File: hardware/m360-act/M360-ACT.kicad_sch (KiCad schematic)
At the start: 26 parts, among them J1 5V do quadro, J2 M360-RF, J3 RJ45 RELES-A, J4 RJ45 RELES-B, J5 RJ45 SENSORES, SW1 Repareamento, U1 AMS1117-3.3, U2 74HCT244, U3 CD74HC4067, U4 SRV05-4, U5 SRV05-4, U6 SRV05-4, U7 SRV05-4, U8 SRV05-4

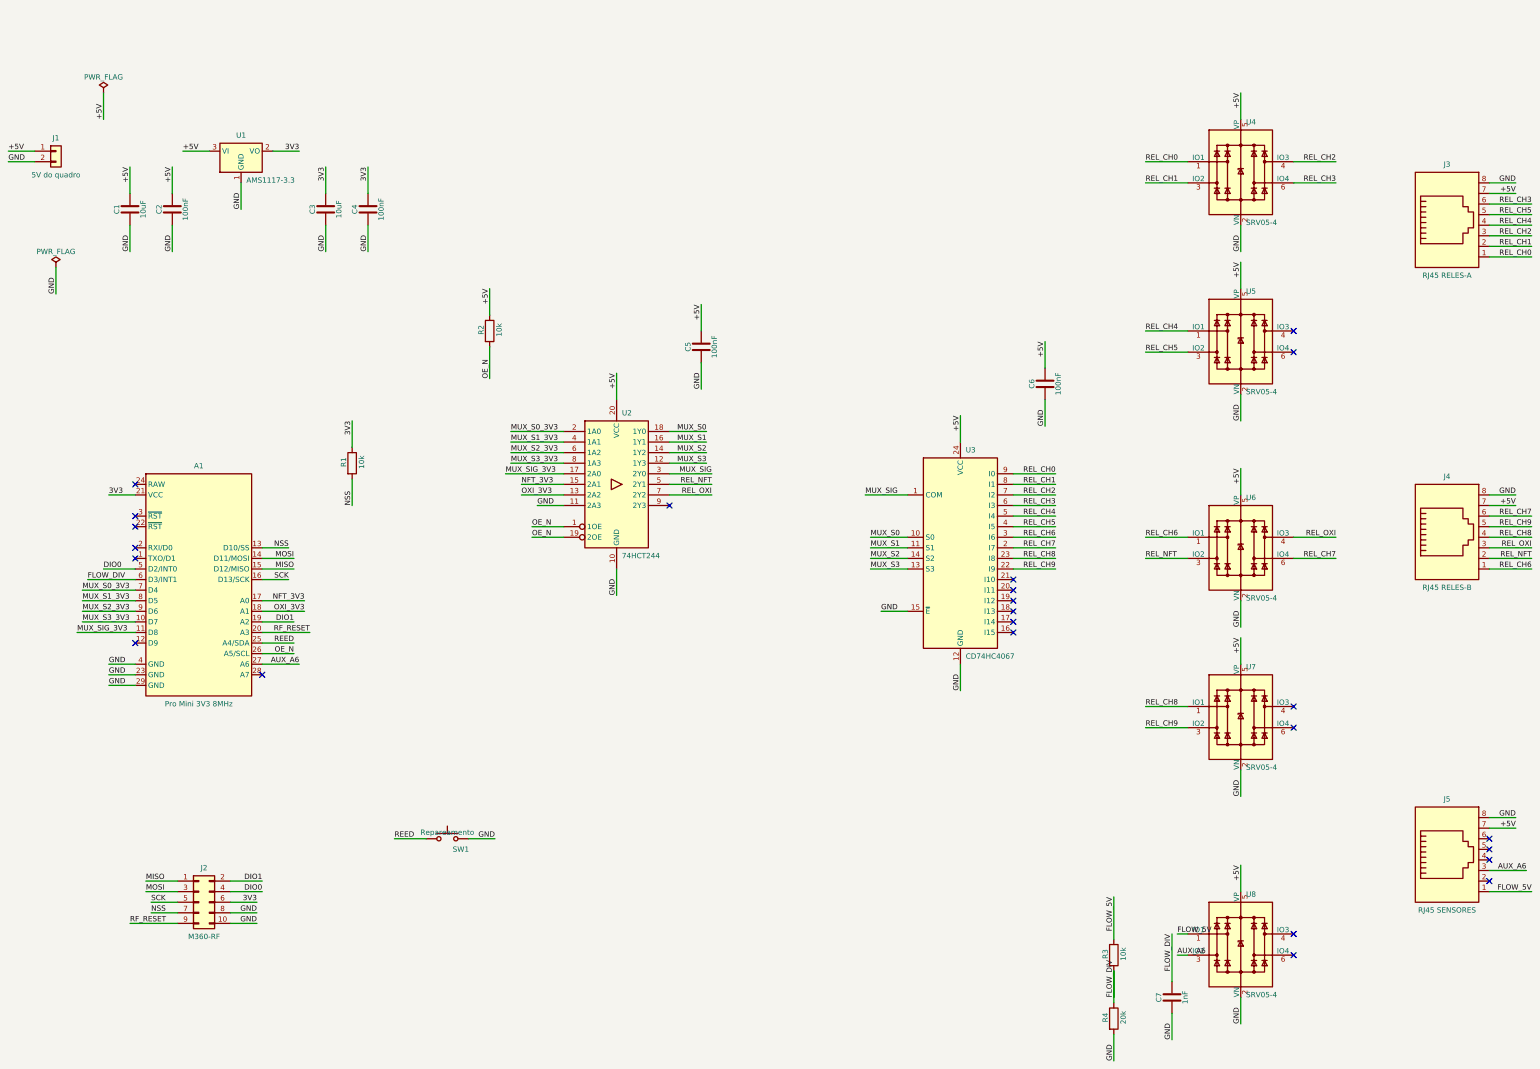
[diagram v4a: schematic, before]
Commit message: feat(hardware): esquemáticos corrigidos após análise adversarial; reed nas três placas; GW em SMD
⚠️ **Só esquemáticos.** Os três .kicad_pcb estão defasados e serão refeitos depois de uma nova
análise adversarial, até zerar os achados (pedido do usuário). ARQUITETURA §9 registra.

Correções da revisão (Fable 5.1, 2026-09-13):
- ACT #1: A6 da J5 com divisor 10 k (R5) / 20 k (R6) + 100 nF (C8); J5.3 e U8.3 vão para AUX_A6_IN.
  Antes, 5 V do par marrom chegavam direto ao ADC6 de um ATmega a 3,3 V.
- ACT #2: pull-up do /OE (R2) de +5V para 3V3 — A5 em alta impedância ficava a ~3,8 V.
- ACT #4: 7× 100 kΩ — pull-down em MUX_S0..S3, pull-up para 5 V em MUX_SIG/REL_NFT/REL_OXI.
- ACT #6: AMS1117 → ME6211C33M5 (C82942), estável com cerâmico.
- ACT #12: AO3401A (Q1) contra inversão no borne; J1.1 vai para VIN_RAW.
- GW #5/#12: Schottky SS14 (D1, C2480) em série de J2.1 (VIN_RAW) para +5V.
- Achados 3, 7, 8, 9, 10 e 11: documentação e regras de firmware (módulo TP4056 com DW01+8205;
  vazão com INPUT; calibração e analogReference do A6 da LP; chave do mezanino cortando o pino 10;
  FTDI sem VCC; orçamento do 3,3 V da GW).

Decisões do usuário:
- Reed switch Littelfuse 59170 (C315909) de volta na LP e na ACT e **no lugar do botão AP/reset da
  GW**, pela PCBA. Símbolo trocado por texto (pinagem idêntica): netlists idênticas.
- GW em SMD pela JLCPCB: R 0603, C1 10 µF 0805 (`Device:C`), C2–C4 100 nF 0603, códigos basic.
  Solda manual só U1 (D1 mini), J1, J2, J3. Os PWR_FLAG saem do BOM.
- Solda manual marcada só nos esquemáticos (`solda_manual.py --so-esquematico`, e `--desfazer` no
  SW1): LP J3; ACT J1; GW U1, J1, J2, J3.

Verificado nas três: netdiff contra a base lista só as mudanças acima (LP idêntica); campos de
todos os componentes comparados; símbolos de biblioteca embutidos comparados com o HEAD; ERC 0;
BOM com código LCSC em todas as linhas (exceto módulos); desenho conferido em PDF.

Três armadilhas medidas no caminho (ARQUITETURA §12):
- `replace_schematic_component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
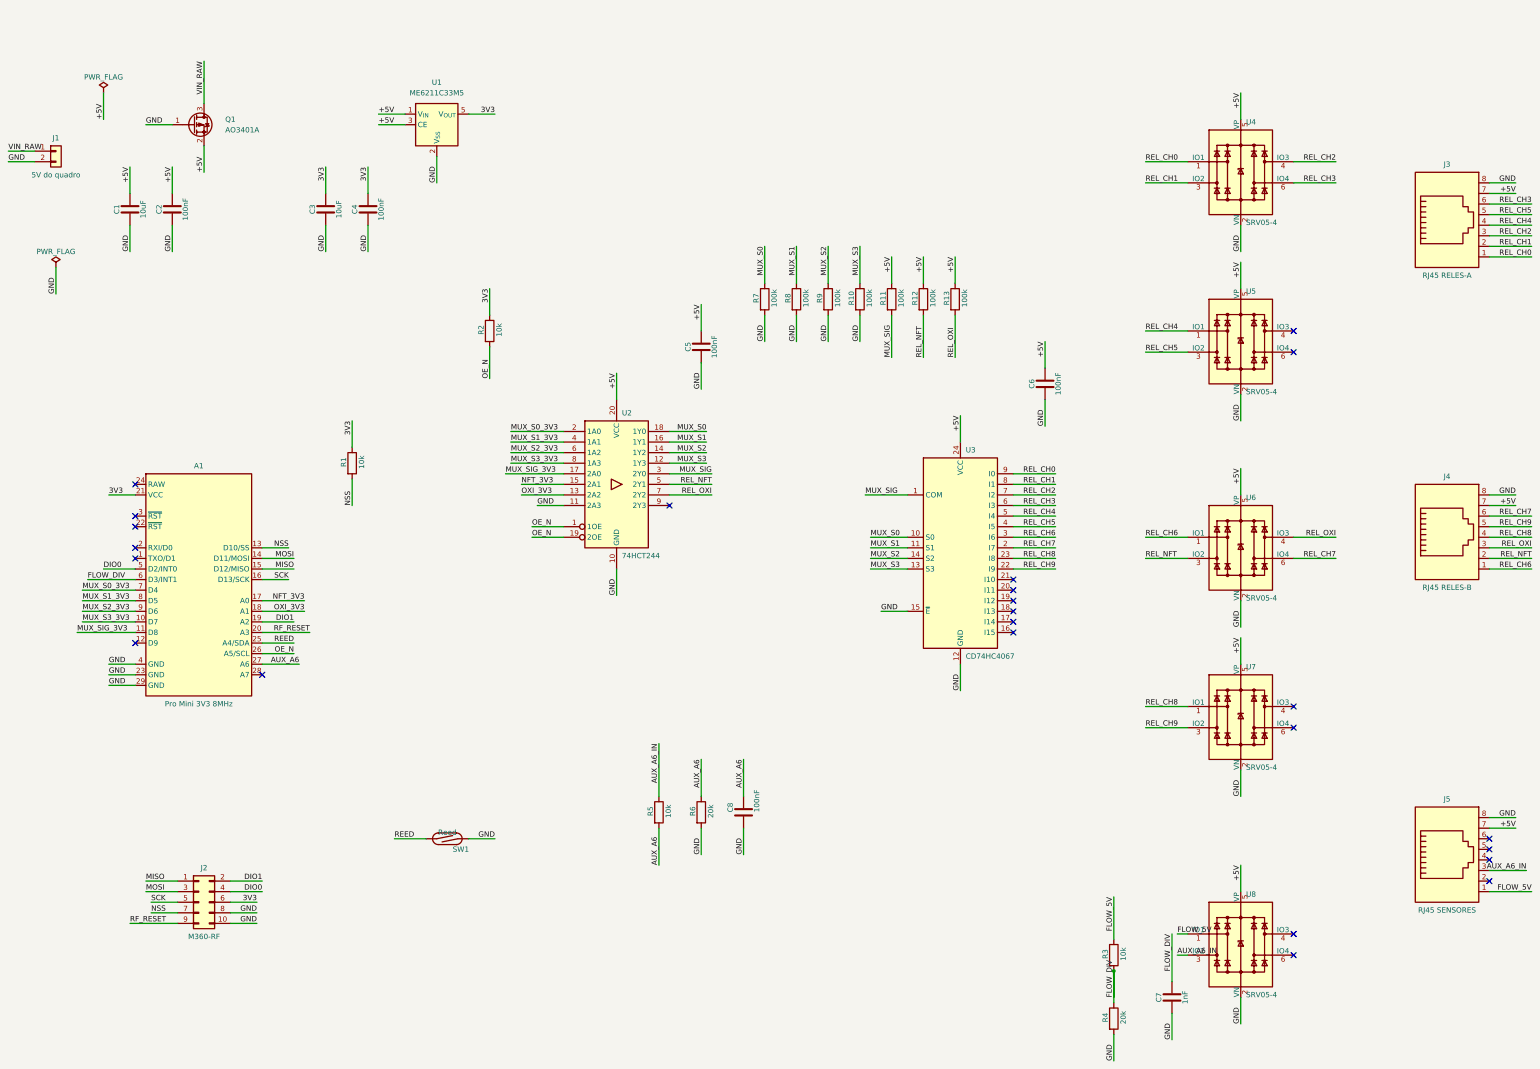
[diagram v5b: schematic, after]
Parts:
- removed U1: AMS1117-3.3, Package_TO_SOT_SMD:SOT-223-3_TabPin2, symbol Regulator_Linear:AMS1117-3.3
- added C8: 100nF, Capacitor_SMD:C_0603_1608Metric, symbol Device:C
- added Q1: AO3401A, Package_TO_SOT_SMD:SOT-23, symbol Transistor_FET:AO3401A
- added R10, R11, R12, R13, R7, R8, R9: 100k, Resistor_SMD:R_0603_1608Metric, symbol Device:R
- added R5: 10k, Resistor_SMD:R_0603_1608Metric, symbol Device:R
- added R6: 20k, Resistor_SMD:R_0603_1608Metric, symbol Device:R
- added U1: ME6211C33M5, Package_TO_SOT_SMD:SOT-23-5, symbol Regulator_Linear:ME6211C33M5
- J1: now left out of the parts list
- SW1: value Repareamento -> Reed; footprint Button_Switch_THT:SW_PUSH_6mm -> M360:Reed_Littelfuse_59170; symbol Switch:SW_Push -> Switch:SW_Reed; LCSC C393938 -> C315909; now in the parts list
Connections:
- net +5V: now also Q1.2 (S), R11.1, R12.1, R13.1, U1.1 (V_{IN}), U1.3 (CE); no longer J1.1 (Pin_1), R2.1
- net 3V3: now also R2.1, U1.5 (V_{OUT})
- net AUX_A6: now also C8.1, R5.2, R6.1; no longer J5.3, U8.3 (IO2)
- net GND: now also C8.2, Q1.1 (G), R10.2, R6.2, R7.2, R8.2, R9.2, U1.2 (V_{SS})
- net MUX_S0: now also R7.1
- net MUX_S1: now also R8.1
- net MUX_S2: now also R9.1
- net MUX_S3: now also R10.1
- net MUX_SIG: now also R11.2
- net REL_NFT: now also R12.2
- net REL_OXI: now also R13.2
- new net AUX_A6_IN: J5.3, R5.1, U8.3 (IO2)
- new net VIN_RAW: J1.1 (Pin_1), Q1.3 (D)

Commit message: fix(hardware): esquemáticos — correções da 2ª análise adversarial
⚠️ Só esquemáticos; as placas continuam defasadas de propósito até zerar os achados.

- LP #1 (firmware + documento): a referência DEFAULT é o VCC, e abaixo de ~3,31 V de bateria o
  MCP1700 sai de regulação — o A6 devolve sempre "3,3 V". O firmware corrige pelo VCC medido no
  bandgap (`readADCInternal()` de M360Power.cpp): VBAT = 3 × ADC_A6 × VCC / 1023. §4.1 e §9.
- ACT #2: entrada da vazão refeita — R3 10 kΩ em série, D1 BAT54WS (C7502694) do D3 para o 3V3,
  R4 de 20 kΩ para 100 kΩ (pull-down, sem pulsos falsos com o sensor desligado). Serve às unidades
  push-pull e às de coletor aberto com pull-up interno, que no divisor antigo davam só 2,5 V.
- ACT #3: R14–R20 100 kΩ nas entradas do 74HCT244 — pull-down em MUX_S0..S3_3V3, pull-up para 3V3
  em MUX_SIG_3V3, NFT_3V3 e OXI_3V3. O /OE cobria as saídas, não as entradas.
- GW #4: Q1 2N7002 (C8545) — o GPIO2 (boot) só comanda o gate; o LED verde vai do 3,3 V ao dreno.
  Curto do chicote para o GND acende o LED em vez de travar o boot. Verde passa a ativo em HIGH,
  como os outros — some a inversão pendente no M360Leds.cpp.
- ACT #5: nota de projeto — o divisor do A6 carrega a fonte com 30 kΩ (§5.2, §7).
- Documento: `MY_RFM95_RST_PIN` (D8 na LP, A3 na ACT) na §9; saem a linha "DHT11 no atuador" da §9
  e o buck XL1509 da §9.1, inconsistentes com a §5.

Verificado: netdiff contra o commit anterior só com as redes previstas (LP idêntica; ACT 10, GW 3);
campos dos componentes existentes inalterados (fora o valor do R4); símbolos de biblioteca
existentes inalterados; ERC 0 nas três; BOM com código LCSC em todas as linhas; desenho conferido
em PDF.

Co-Authored-By: Claude Opus 5 (1M context) <noreply@anthropic.com>
Claude-Session: https://claude.ai/code/session_012t7RkcrXvvpDVjKVimNu18
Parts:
- added D1: BAT54WS, Diode_SMD:D_SOD-323, symbol Device:D_Schottky
- added R14, R15, R16, R17, R18, R19, R20: 100k, Resistor_SMD:R_0603_1608Metric, symbol Device:R
- R4: value 20k -> 100k; LCSC C4184 -> C25803
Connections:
- net 3V3: now also D1.1 (K), R18.1, R19.1, R20.1
- net FLOW_DIV: now also D1.2 (A)
- net GND: now also R14.2, R15.2, R16.2, R17.2
- net MUX_S0_3V3: now also R14.1
- net MUX_S1_3V3: now also R15.1
- net MUX_S2_3V3: now also R16.1
- net MUX_S3_3V3: now also R17.1
- net MUX_SIG_3V3: now also R18.2
- net NFT_3V3: now also R19.2
- net OXI_3V3: now also R20.2

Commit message: fix(hardware): esquemáticos — correções da 3ª análise adversarial
⚠️ Só esquemáticos; as placas continuam defasadas de propósito até zerar os achados.

- LP #1: 100 Ω em série (R26–R29, C22775) entre o TVS e o Pro Mini nas linhas de campo digitais.
  A1.18/19/25/26 passam às redes ONEWIRE_MCU, DHT_MCU, SDA_MCU e SCL_MCU; pull-ups e TVS ficam do
  lado do conector. O pino do ATmega deixa de dividir o surto com o TVS.
- ACT #2: 100 Ω em série (R21–R32) entre o CI e o TVS nas 12 linhas de relé — U3 I0–I9 em
  REL_CHx_MUX, U2 2Y1/2Y2 em REL_NFT_BUF/REL_OXI_BUF. Custa 0,2 V nos 2 mA do opto.
- ACT e GW #3: TVS SMAJ5.0A (D2, C2925443) do +5V ao GND, depois do Q1 (ACT) e do D1 (GW), contra
  DC-DC ajustável girado por engano. Símbolo `Device:D_Zener` — o `D_TVS` do KiCad é bidirecional.
- GW #4: nota — o LED azul do D1 mini no GPIO2 fica invertido em relação ao verde do painel.
- Regras: limiar de corte de TX ≥ 3,0 V por causa do BOD de 2,7 V (efuse 0xFD); confirmar os fuses
  dos clones DeeKRobot por ISP; `initLEDs` com argumentos trocados continua registrado. §9.

Verificado: netdiff contra o commit anterior só com as redes previstas (LP 8, ACT 26, GW 2);
campos dos componentes existentes inalterados; símbolos de biblioteca existentes inalterados
(entra só o D_Zener, sai o D_TVS); ERC 0; BOM com código LCSC em todas as linhas; desenho
conferido em PDF. O diff da LP é grande porque o arquivo passou pela primeira vez por
`kicad-cli sch upgrade --force` (§12).

No caminho: o MCP ignorou o ângulo pedido em `add_schematic_component` (todas as peças entraram em
rot 0) e, com as fileiras apertadas, os fios desenhados fundiram redes — o netdiff e o ERC pegaram,
e a geometria foi refeita antes do commit.

Co-Authored-By: Claude Opus 5 (1M context) <noreply@anthropic.com>
Claude-Session: https://claude.ai/code/session_012t7RkcrXvvpDVjKVimNu18
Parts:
- added D2: SMAJ5.0A, Diode_SMD:D_SMA, symbol Device:D_Zener
- added R21, R22, R23, R24, R25, R26, R27, R28, R29, R30, R31, R32: 100, Resistor_SMD:R_0603_1608Metric, symbol Device:R
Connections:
- net +5V: now also D2.1 (K)
- net GND: now also D2.2 (A)
- net REL_CH0: now also R21.2; no longer U3.9 (I0)
- net REL_CH1: now also R22.2; no longer U3.8 (I1)
- net REL_CH2: now also R23.2; no longer U3.7 (I2)
- net REL_CH3: now also R24.2; no longer U3.6 (I3)
- net REL_CH4: now also R25.2; no longer U3.5 (I4)
- net REL_CH5: now also R26.2; no longer U3.4 (I5)
- net REL_CH6: now also R27.2; no longer U3.3 (I6)
- net REL_CH7: now also R28.2; no longer U3.2 (I7)
- net REL_CH8: now also R29.2; no longer U3.23 (I8)
- net REL_CH9: now also R30.2; no longer U3.22 (I9)
- net REL_NFT: now also R31.2; no longer U2.5 (2Y1)
- net REL_OXI: now also R32.2; no longer U2.7 (2Y2)
- new net REL_CH0_MUX: R21.1, U3.9 (I0)
- new net REL_CH1_MUX: R22.1, U3.8 (I1)
- new net REL_CH2_MUX: R23.1, U3.7 (I2)
- new net REL_CH3_MUX: R24.1, U3.6 (I3)
- new net REL_CH4_MUX: R25.1, U3.5 (I4)
- new net REL_CH5_MUX: R26.1, U3.4 (I5)
- new net REL_CH6_MUX: R27.1, U3.3 (I6)
- new net REL_CH7_MUX: R28.1, U3.2 (I7)
- new net REL_CH8_MUX: R29.1, U3.23 (I8)
- new net REL_CH9_MUX: R30.1, U3.22 (I9)
- new net REL_NFT_BUF: R31.1, U2.5 (2Y1)
- new net REL_OXI_BUF: R32.1, U2.7 (2Y2)

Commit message: fix(hardware): PTC na entrada de 5 V da ACT e da GW — correções da 4ª análise adversarial
⚠️ Só esquemáticos; as placas continuam defasadas de propósito até zerar os achados.

- ACT e GW #1: PTC F1 500 mA / 30 V (Jinrui JK-nSMD050-30, C720075) em série na entrada, depois do
  Q1 (ACT) e do SS14 (GW) e antes do TVS D2 — Q1.2 e D1.1 passam à rede VIN_POL. A ruptura mínima
  do SMAJ5.0A (6,4 V) fica acima da dos SRV05-4 (6,0 V), então sozinho o D2 não tirava os TVS de
  sinal do papel sacrificial; com o F1 a montante, a condução do D2 abre o circuito. O F1 cobre
  também o curto no chicote (a placa desarma, o quadro não cai) — §9 revista.
  Escolhido no lugar do SMD1206P050TF/15 (C106264) sugerido: mesma especificação, 427 mil em
  estoque contra 1 350, e resistência máxima de 300 mΩ contra 750 mΩ.
- ACT #2: procedimento — barramento de 5 V do quadro ajustado em 5,0 V (máx. 5,1 V), na §5.1.
- Pino 1 do RJ45: verificado por geometria e convenção pela revisão; registrada na §9 a medida de
  continuidade na primeira placa (branco-laranja T568B ↔ pad 1) antes de crimpar os chicotes.

Verificado: netdiff só com as duas redes previstas em cada placa; campos e símbolos de biblioteca
existentes inalterados (entra o Polyfuse); ERC 0; BOM com código LCSC em todas as linhas; desenho
conferido em PDF.

Co-Authored-By: Claude Opus 5 (1M context) <noreply@anthropic.com>
Claude-Session: https://claude.ai/code/session_012t7RkcrXvvpDVjKVimNu18
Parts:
- added F1: 500mA, Fuse:Fuse_1206_3216Metric, symbol Device:Polyfuse
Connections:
- net +5V: now also F1.2; no longer Q1.2 (S)
- new net VIN_POL: F1.1, Q1.2 (S)
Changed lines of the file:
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@@
 	(wire
 		(pts
+			(xy 66.04 33.02) (xy 66.04 22.86)
+		)
+		(stroke
+			(width 0)
+			(type default)
+		)
+	)
+	(wire
+		(pts
 			(xy 298.45 243.84) (xy 298.45 232.41)
 		)
@@
 	(wire
 		(pts
-			(xy 66.04 33.02) (xy 66.04 22.86)
-		)
-		(stroke
-			(width 0)
-			(type default)
-		)
-	)
-	(wire
-		(pts
-			(xy 66.04 43.18) (xy 66.04 49.53)
-		)
-		(stroke
-			(width 0)
-			(type default)
-		)
-	)
-	(wire
-		(pts
 			(xy 208.28 229.87) (xy 208.28 223.52)
 		)
@@
 	(wire
 		(pts
+			(xy 58.42 38.1) (xy 52.07 38.1)
+		)
+		(stroke
+			(width 0)
+			(type default)
+		)
+	)
+	(wire
+		(pts
 			(xy 327.66 46.99) (xy 337.82 46.99)
 		)
@@
 	(wire
 		(pts
+			(xy 81.28 59.69) (xy 81.28 66.04)
+		)
+		(stroke
+			(width 0)
+			(type default)
+		)
+	)
+	(wire
+		(pts
 			(xy 284.48 241.3) (xy 284.48 247.65)
 		)
@@
 	(wire
 		(pts
-			(xy 58.42 38.1) (xy 52.07 38.1)
-		)
-		(stroke
-			(width 0)
-			(type default)
-		)
-	)
-	(wire
-		(pts
 			(xy 156.21 33.02) (xy 142.24 33.02)
 		)
@@
 	(wire
 		(pts
+			(xy 66.04 43.18) (xy 66.04 53.34)
+		)
+		(stroke
+			(width 0)
+			(type default)
+		)
+	)
+	(wire
+		(pts
 			(xy 152.4 137.16) (xy 144.78 137.16)
 		)
@@
 	(wire
 		(pts
+			(xy 81.28 52.07) (xy 81.28 41.91)
+		)
+		(stroke
+			(width 0)
+			(type default)
+		)
+	)
+	(wire
+		(pts
 			(xy 314.96 62.23) (xy 314.96 68.58)
 		)
@@
 		)
 	)
+	(label "VIN_POL"
+		(at 81.28 41.91 270)
+		(effects
+			(font
+				(size 1.27 1.27)
+			)
+			(justify right bottom)
+		)
+	)
 	(label "MUX_S1_3V3"
 		(at 170.18 217.17 270)
@@
 		)
 	)
-	(label "+5V"
-		(at 66.04 49.53 90)
-		(effects
-			(font
-				(size 1.27 1.27)
-			)
-			(justify left bottom)
-		)
-	)
 	(label "MOSI"
 		(at 52.07 222.25 0)
@@
 		)
 	)
+	(label "VIN_RAW"
+		(at 66.04 22.86 270)
+		(effects
+			(font
+				(size 1.27 1.27)
+			)
+			(justify right bottom)
+		)
+	)
 	(label "FLOW_5V"
 		(at 284.48 223.52 270)
@@
 		)
 	)
+	(label "GND"
+		(at 52.07 38.1 0)
+		(effects
+			(font
+				(size 1.27 1.27)
+			)
+			(justify left bottom)
+		)
+	)
 	(label "REL_NFT_BUF"
 		(at 187.96 124.46 180)
@@
 	)
 	(label "GND"
-		(at 52.07 38.1 0)
-		(effects
-			(font
-				(size 1.27 1.27)
-			)
-			(justify left bottom)
-		)
-	)
-	(label "GND"
 		(at 298.45 257.81 90)
 		(effects
@@
 		)
 	)
+	(label "VIN_POL"
+		(at 66.04 53.34 90)
+		(effects
+			(font
+				(size 1.27 1.27)
+			)
+			(justify left bottom)
+		)
+	)
 	(label "MUX_S3_3V3"
 		(at 36.83 157.48 0)
@@
 		)
 	)
+	(label "+5V"
+		(at 81.28 66.04 90)
+		(effects
+			(font
+				(size 1.27 1.27)
+			)
+			(justify left bottom)
+		)
+	)
 	(label "REL_CH8"
 		(at 255.27 17.78 180)
@@
 		)
 	)
-	(label "VIN_RAW"
-		(at 66.04 22.86 270)
-		(effects
-			(font
-				(size 1.27 1.27)
-			)
-			(justify right bottom)
-		)
-	)
 	(label "REL_CH3"
 		(at 173.99 40.64 180)
@@
 					(unit 1)
 				)
+			)
+		)
+	)
+	(symbol
+		(lib_id "Device:Polyfuse")
+		(at 81.28 55.88 0)
+		(unit 1)
+		(body_style 1)
+		(exclude_from_sim no)
+		(in_bom yes)
+		(on_board yes)
+		(in_pos_files yes)
+		(dnp no)
+		(property "Reference" "F1"
+			(at 87.63 54.61 0)
+			(show_name no)
+			(do_not_autoplace no)
+			(effects
+				(font
+					(size 1.27 1.27)
+				)
+			)
+		)
+		(property "Value" "500mA"
+			(at 87.63 57.15 0)
+			(show_name no)
+			(do_not_autoplace no)
+			(effects
+				(font
+					(size 1.27 1.27)
+				)
+			)
+		)
+		(property "Footprint" "Fuse:Fuse_1206_3216Metric"
+			(at 81.28 55.88 0)
+			(hide yes)
+			(show_name no)
+			(do_not_autoplace no)
+			(effects
+				(font
+					(size 1.27 1.27)
+				)
+				(justify left)
+			)
+		)
+		(property "Datasheet" ""
+			(at 81.28 55.88 0)
+			(hide yes)
+			(show_name no)
+			(do_not_autoplace no)
+			(effects
+				(font
+					(size 1.27 1.27)
+				)
+			)
+		)
+		(property "Description" "Resettable fuse, polymeric positive temperature coefficient"
+			(at 81.28 55.88 0)
+			(hide yes)
+			(show_name no)
+			(do_not_autoplace no)
+			(effects
+				(font
+					(size 1.27 1.27)
+				)
+			)
+		)
+		(property "LCSC" "C720075"
+			(at 81.28 55.88 0)
+			(hide yes)
+			(show_name no)
+			(do_not_autoplace no)
+			(effects
+				(font
+					(size 1.27 1.27)
+				)
+			)
+		)
+		(pin "1"
+		)
+		(pin "2"
+		)
+		(instances
+			(project "M360-ACT"
+				(path "/c5ce62f1-25ea-4dcc-94a9-6f847c324d30"
+					(reference "F1")
+					(unit 1)
+				)
